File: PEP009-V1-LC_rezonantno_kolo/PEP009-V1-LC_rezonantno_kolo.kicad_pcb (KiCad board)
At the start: 2 copper layers, 45 x 45 mm, 13 parts, among them J1 Screw_Terminal_01x02

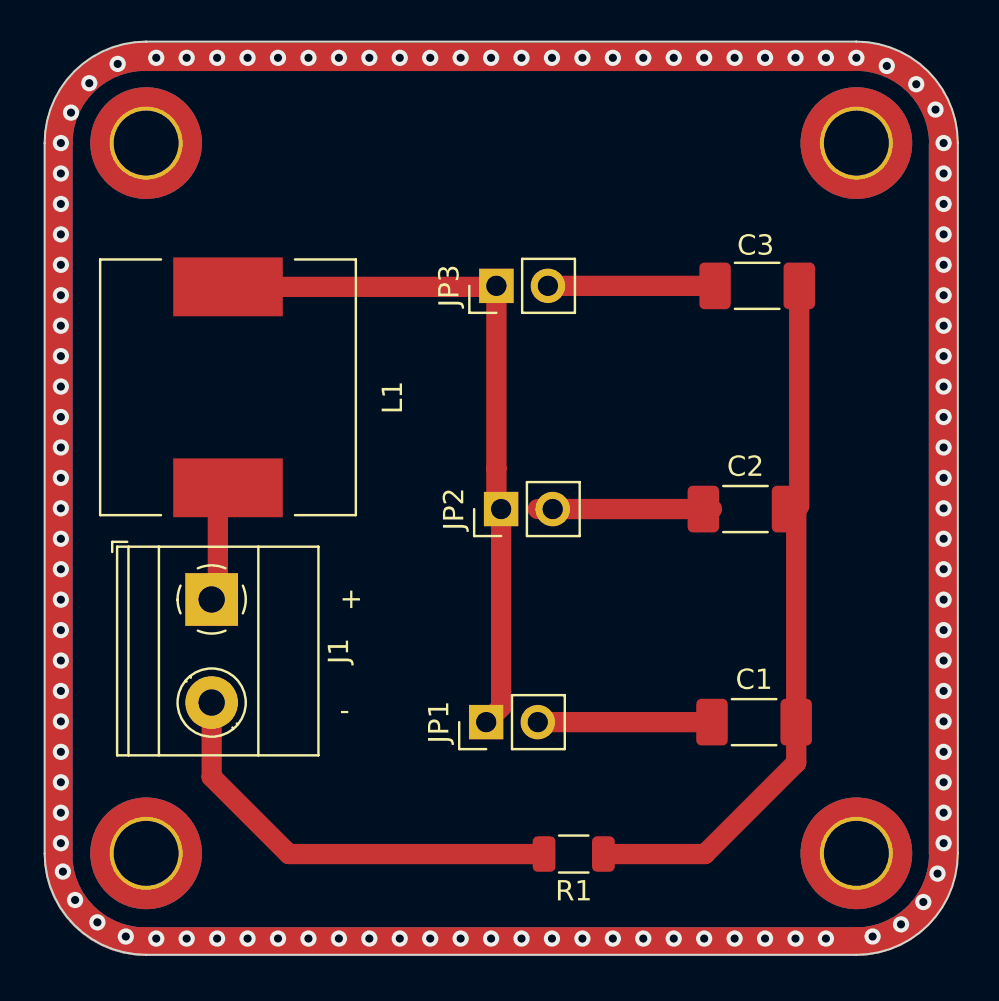
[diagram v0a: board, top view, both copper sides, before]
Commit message: PEP006 and PEP009 update.
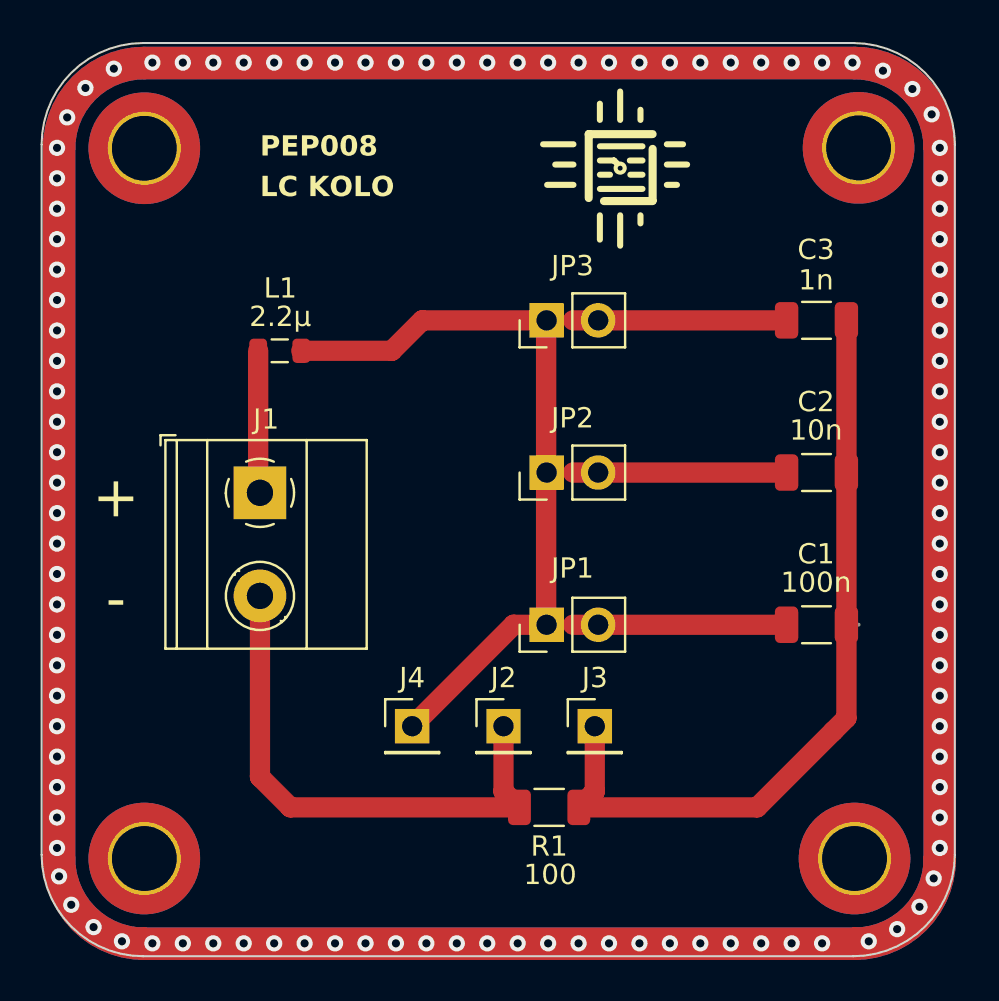
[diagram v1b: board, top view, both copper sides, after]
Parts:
- added G***: LOGO, logo:logo, B.Cu at (137.8, 75.9)
- added J2: Conn_01x01_Pin, Connector_PinHeader_2.54mm:PinHeader_1x01_P2.54mm_Vertical, F.Cu at (143.6, 101.2)
- added J3: Conn_01x01_Pin, Connector_PinHeader_2.54mm:PinHeader_1x01_P2.54mm_Vertical, F.Cu at (148.1, 101.2)
- added J4: Conn_01x01_Pin, Connector_PinHeader_2.54mm:PinHeader_1x01_P2.54mm_Vertical, F.Cu at (139.1, 101.2)
- added REF**: JP_silk_symbol, PEP_library:JP_silk_symbol, F.Cu at (147.0, 83.4)
- added REF**: JP_silk_symbol, PEP_library:JP_silk_symbol, F.Cu at (147.0, 98.4)
- added REF**: JP_silk_symbol, PEP_library:JP_silk_symbol, F.Cu at (147.0, 90.8)
- added REF**: ele_petnica_logo, PEP_library:ele_petnica_logo, F.Cu at (149.3, 73.7)
- C1, C2, C3: footprint Capacitor_SMD:C_1808_4520Metric -> Capacitor_SMD:C_1206_3216Metric
- L1: value 220µ -> 2.2µ; footprint Inductor_SMD:L_12x12mm_H4.5mm -> Inductor_SMD:L_0805_2012Metric
- moved J1 5.77 mm to (131.6, 89.7)
- moved C1 5.70 mm to (159.0, 96.2)
- moved JP1 5.65 mm to (145.7, 96.2)
- moved C2 3.94 mm to (159.0, 88.7)
- moved C3 3.38 mm to (159.0, 81.2)
- moved L1 3.12 mm to (132.6, 82.7), turned to 0 degrees
- moved JP3 3.00 mm to (145.7, 81.2)
- moved JP2 2.87 mm to (145.7, 88.7)
- moved R1 2.60 mm to (145.8, 105.2)
- moved H4 0.27 mm to (160.9, 107.7)
- moved H2 0.27 mm to (125.9, 72.7)
- moved H1 0.27 mm to (125.9, 107.7)
- moved H3 0.26 mm to (161.1, 72.7)
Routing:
- net GND: track 21.6 -> 26.7 mm
- net Net-(J3-Pin_1): track 35.0 -> 38.9 mm
- net Net-(JP3-B): track 8.24 -> 10.5 mm
- net Net-(JP2-B): track 8.59 -> 10.5 mm
- net Net-(JP1-B): track 8.59 -> 10.5 mm
- net Input voltage: track 5.84 -> 7.04 mm
- net (no net): track 0.00 -> 0.50 mm, vias 0 -> 109
- net 0: vias 109 -> 0
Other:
- board text added: "100"
- board text added: "100n"
- board text added: "10n"
- board text added: "1n"
- board text added: "2.2µ"
- board text added: "Kontakti za merenje"
- board text added: "LC KOLO"
- board text added: "PEP008"
